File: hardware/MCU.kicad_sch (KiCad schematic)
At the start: 33 parts, among them J1 USB_C_Receptacle_USB2.0_16P, J2 Conn_01x06, J8 Conn_02x02_Odd_Even, J9 Conn_01x06, U1 W25Q128JVS, U2 RP2350A, Y1 ABM8-272-T3

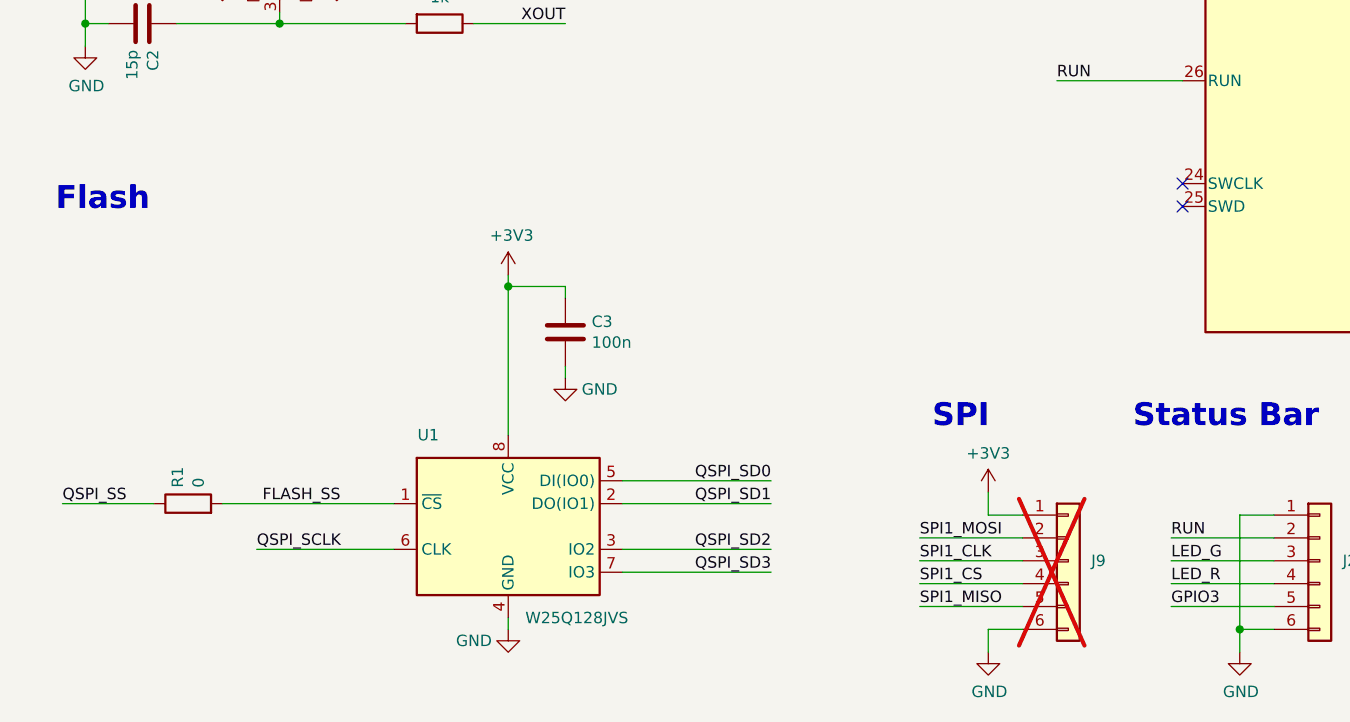
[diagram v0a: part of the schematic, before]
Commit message: feat: add SWD footprint
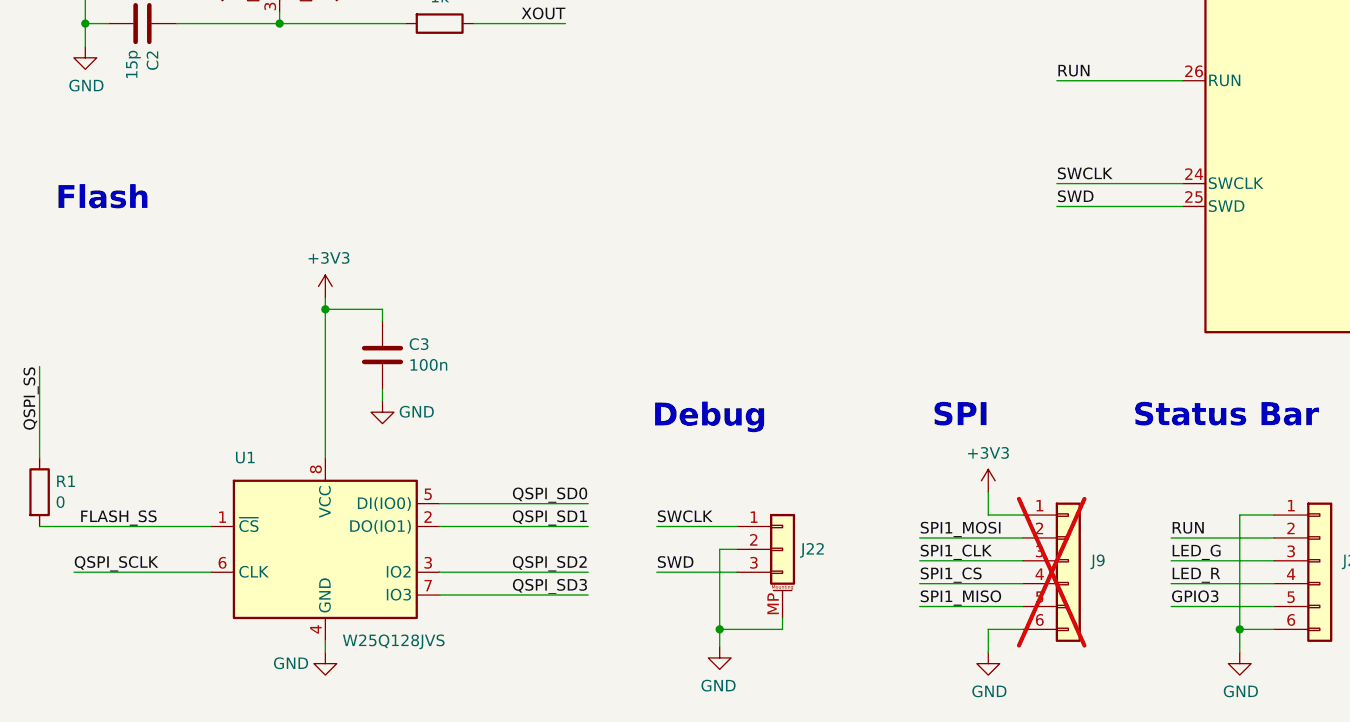
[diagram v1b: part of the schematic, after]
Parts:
- added J22: SM03B-SRSS-TB, Connector_JST:JST_SH_SM03B-SRSS-TB_1x03-1MP_P1.00mm_Horizontal, symbol Connector_Generic_MountingPin:Conn_01x03_MountingPin
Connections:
- net GND: now also J22.2 (Pin_2), J22.MP (MountPin)
- net SWCLK: now reaches U2.24 (SWCLK)
- net SWCLK: now also J22.1 (Pin_1)
- net SWD: now reaches U2.25 (SWD)
- net SWD: now also J22.3 (Pin_3)
- no-connect marks 11 -> 9
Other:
- note added: "Debug"
- moved on the sheet: C3, R1, U1
